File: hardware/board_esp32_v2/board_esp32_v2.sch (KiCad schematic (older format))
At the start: 96 parts, among them J1 USB_B_Micro, J2 Conn_01x02, J3 Micro_SD_Card_Det_Hirose_DM3AT, Q1 AO3401, Q2 AO3400, Q3 AO3401, SW1 SW_Push-Std, U1 FT231XS, U2 ESP32-WROOM-32D, U3 E22-900M22S, U4 E22-900M30S, U5 TPS62162DGK

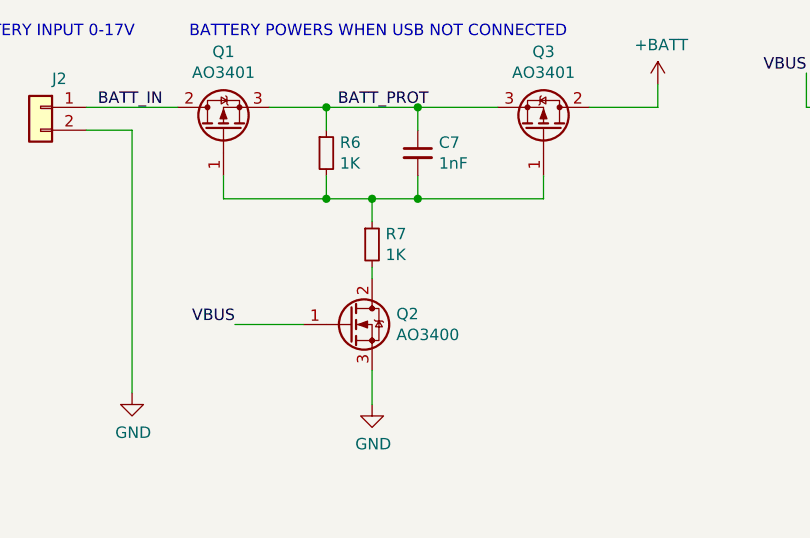
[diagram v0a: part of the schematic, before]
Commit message: Finish implementing fixes and pin changes for board_esp32_v2.
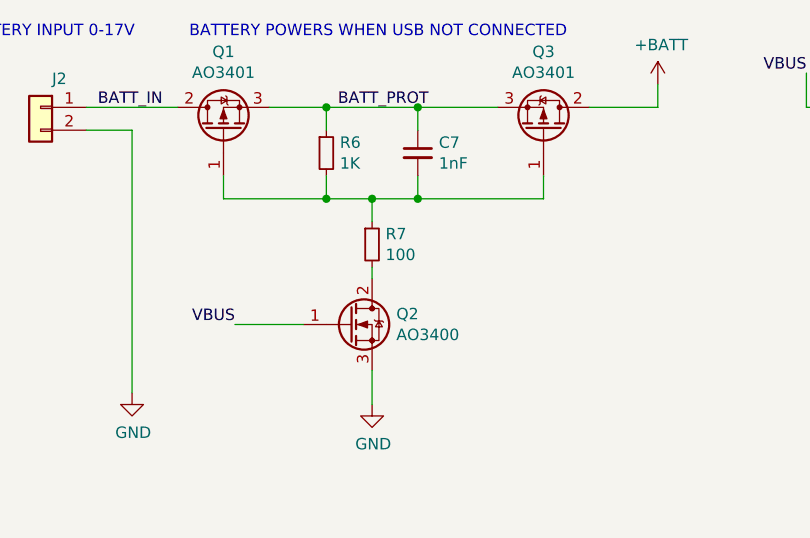
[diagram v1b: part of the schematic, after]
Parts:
- R7: value 1K -> 100
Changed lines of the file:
@@
-EESchema Schematic File Version 5
-EELAYER 32 0
+EESchema Schematic File Version 4
+EELAYER 30 0
 EELAYER END
 $Descr A3 16535 11693
@@
 Comment3 ""
 Comment4 ""
-Comment5 ""
-Comment6 ""
-Comment7 ""
-Comment8 ""
-Comment9 ""
 $EndDescr
 Connection ~ 13100 1350
@@
 P 4750 1650
 F 0 "R7" H 4809 1696 50  0000 L CNN
-F 1 "1K" H 4809 1605 50  0000 L CNN
+F 1 "100" H 4809 1605 50  0000 L CNN
 F 2 "Resistor_SMD:R_0402_1005Metric" H 4750 1650 50  0001 C CNN
 F 3 "~" H 4750 1650 50  0001 C CNN

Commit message: adds board_esp32_v3
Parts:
- removed U2: ESP32-WROOM-32D, RF_Module:ESP32-WROOM-32, symbol RF_Module:ESP32-WROOM-32D
- added JP42: SolderJumper_2_Open, Jumper:SolderJumper-2_P1.3mm_Open_RoundedPad1.0x1.5mm, symbol Jumper:SolderJumper_2_Open
- added TP5, TP6, TP7, TP8: TP_HOLE, Connector_PinHeader_2.54mm:PinHeader_1x01_P2.54mm_Vertical, symbol fitz_parts:TP_HOLE
- added U2: ESP32-WROOM-32U, RF_Module:ESP32-WROOM-32U, symbol RF_Module:ESP32-WROOM-32U
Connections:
- net labels removed: LORA1_TXEN, LORA2_TXEN
- wire segments 284 -> 290
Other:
- note added: "Possible Connection\nto save GPIO"
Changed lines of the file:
@@
-EESchema Schematic File Version 4
-EELAYER 30 0
+EESchema Schematic File Version 5
+EELAYER 34 0
 EELAYER END
 $Descr A3 16535 11693
@@
 Comment3 ""
 Comment4 ""
+Comment5 ""
+Comment6 ""
+Comment7 ""
+Comment8 ""
+Comment9 ""
 $EndDescr
+Connection ~ 1150 3900
+Connection ~ 1200 7400
+Connection ~ 1200 8000
+Connection ~ 1250 1750
+Connection ~ 1300 4000
+Connection ~ 1700 7350
+Connection ~ 1700 7400
+Connection ~ 2550 7150
+Connection ~ 2600 3000
+Connection ~ 2600 5400
+Connection ~ 3000 6450
+Connection ~ 3000 7150
+Connection ~ 3500 3000
+Connection ~ 3500 5000
+Connection ~ 3750 6450
+Connection ~ 4550 1050
+Connection ~ 4550 1450
+Connection ~ 4750 1450
+Connection ~ 4800 7150
+Connection ~ 4800 7350
+Connection ~ 4950 1050
+Connection ~ 4950 1450
+Connection ~ 5150 9350
+Connection ~ 5350 8350
+Connection ~ 5350 8450
+Connection ~ 5350 8750
+Connection ~ 8250 3450
+Connection ~ 8250 6200
+Connection ~ 8250 6250
+Connection ~ 8850 3450
+Connection ~ 8850 6200
+Connection ~ 11500 1350
+Connection ~ 11700 1350
+Connection ~ 12150 2150
+Connection ~ 12250 2150
+Connection ~ 12500 4950
 Connection ~ 13100 1350
 Connection ~ 13350 1350
 Connection ~ 13900 1350
-Connection ~ 11700 1350
-Connection ~ 11500 1350
-Connection ~ 12500 4950
-Connection ~ 8250 6250
-Connection ~ 8850 6200
-Connection ~ 8250 6200
-Connection ~ 8850 3450
-Connection ~ 8250 3450
-Connection ~ 1250 1750
-Connection ~ 2600 3000
-Connection ~ 1300 4000
-Connection ~ 1150 3900
-Connection ~ 3500 3000
-Connection ~ 4950 1050
-Connection ~ 4550 1050
-Connection ~ 4950 1450
-Connection ~ 4750 1450
-Connection ~ 4550 1450
-Connection ~ 3500 5000
-Connection ~ 2600 5400
-Connection ~ 3000 6450
-Connection ~ 3000 7150
-Connection ~ 2900 7150
-Connection ~ 3750 6450
-Connection ~ 4800 7150
-Connection ~ 4800 7350
-Connection ~ 5150 9350
-Connection ~ 5350 8750
-Connection ~ 1200 8000
-Connection ~ 1700 7350
-Connection ~ 1200 7400
-Connection ~ 1700 7400
-Connection ~ 5350 8450
-Connection ~ 5350 8350
-Connection ~ 12150 2150
-Connection ~ 12250 2150
+NoConn ~ 3150 8550
 NoConn ~ 9600 7450
+NoConn ~ 3150 8350
 NoConn ~ 9600 4700
+NoConn ~ 3150 8450
+NoConn ~ 3150 8850
 NoConn ~ 3150 8750
-NoConn ~ 3150 8850
-NoConn ~ 3150 8350
-NoConn ~ 3150 8450
-NoConn ~ 3150 8550
 NoConn ~ 3150 8650
 Wire Wire Line
@@
 	2150 1750 2150 1850
 Wire Wire Line
+	2350 7150 2550 7150
+Wire Wire Line
 	2400 1050 2400 1450
 Wire Wire Line
 	2400 1850 2400 1750
 Wire Wire Line
-	2500 7150 2900 7150
+	2550 7150 2550 7350
+Wire Wire Line
+	2550 7150 3000 7150
+Wire Wire Line
+	2550 7350 2300 7350
 Wire Wire Line
 	2600 2900 2600 3000
@@
 	2800 5400 2600 5400
 Wire Wire Line
-	2900 7150 2900 7350
-Wire Wire Line
-	2900 7150 3000 7150
-Wire Wire Line
-	2900 7350 2300 7350
-Wire Wire Line
 	3000 6350 3000 6450
 Wire Wire Line
@@
 	3000 7150 3150 7150
 Wire Wire Line
+	3000 7350 3150 7350
+Wire Wire Line
+	3000 7450 3150 7450
+Wire Wire Line
 	3400 3600 3500 3600
 Wire Wire Line
@@
 	6000 950  6000 1050
 Wire Wire Line
+	6150 5550 6150 5650
+Wire Wire Line
+	6150 5650 6250 5650
+Wire Wire Line
 	6650 900  6650 1050
 Wire Wire Line
 	6650 1050 6850 1050
+Wire Wire Line
+	6650 5550 6650 5650
+Wire Wire Line
+	6650 5650 6550 5650
 Wire Wire Line
 	7150 1050 7350 1050
@@
 Text Notes 4500 6550 0    50   ~ 0
 TODO: \n-DOUBLE CHECK RX/TX dir\n-set BATT div to match battery\n- DOUBLE CHECK SPI CS
+Text Notes 5700 5350 0    50   ~ 0
+Possible Connection\nto save GPIO
 Text Notes 8000 5600 0    50   ~ 0
 NOTE: E22-900M22S MAX CURRENT 119mA\nVin 1.8-3.7V
@@
 Text Label 1900 3650 2    50   ~ 0
 FT_3V3
-Text Label 2500 7150 2    50   ~ 0
+Text Label 2350 7150 2    50   ~ 0
 FT_RTS
 Text Label 2800 3000 0    50   ~ 0
@@
 LORA1_NSS
 Text Label 4450 8250 0    50   ~ 0
-LORA2_DIO2
+LORA2_DIO1
 Text Label 4450 8350 0    50   ~ 0
 VSPI_CLK
@@
 VSPI_MISO
 Text Label 4450 8550 0    50   ~ 0
-LORA1_DIO2
+LORA2_RXEN
 Text Label 4450 8650 0    50   ~ 0
 LORA1_BUSY
 Text Label 4450 8750 0    50   ~ 0
 VSPI_MOSI
-Text Label 4450 8850 0    50   ~ 0
-LORA1_TXEN
 Text Label 4450 8950 0    50   ~ 0
-LORA2_RXEN
+LORA1_DIO1
 Text Label 4450 9050 0    50   ~ 0
 LORA1_RXEN
-Text Label 4450 9150 0    50   ~ 0
-LORA2_TXEN
 Text Label 4450 9250 0    50   ~ 0
 LORA2_NSS
@@
 Text Label 5500 8850 0    50   ~ 0
 LORA2_MOSI
+Text Label 6150 5550 2    50   ~ 0
+LORA1_DIO1
 Text Label 6650 900  2    50   ~ 0
 VBUS
+Text Label 6650 5550 0    50   ~ 0
+LORA2_DIO1
 Text Label 7350 9400 0    50   ~ 0
 ESP_LED
@@
 LORA1_RXEN
 Text Label 7550 4250 2    50   ~ 0
-LORA1_TXEN
+LORA1_DIO2
 Text Label 7550 4500 2    50   ~ 0
 LORA1_MOSI
@@
 LORA2_RXEN
 Text Label 7700 7000 2    50   ~ 0
-LORA2_TXEN
+LORA2_DIO2
 Text Label 7700 7250 2    50   ~ 0
 LORA2_MOSI
@@
 LORA2_NSS
 Text Label 8000 9400 0    50   ~ 0
-LORA1_DIO1
+LORA1_DIO2
 Text Label 8650 9400 0    50   ~ 0
-LORA2_DIO1
+LORA2_DIO2
 Text Label 10050 6900 0    50   ~ 0
 LORA2_DIO1
@@
 $EndComp
 $Comp
+L fitz_parts:TP_HOLE TP5
+U 1 1 00000000
+P 3000 7350
+F 0 "TP5" V 3000 7650 50  0000 C CNN
+F 1 "TP_HOLE" H 3000 7550 50  0001 C CNN
+F 2 "Connector_PinHeader_2.54mm:PinHeader_1x01_P2.54mm_Vertical" H 3200 7350 50  0001 C CNN
+F 3 "~" H 3200 7350 50  0001 C CNN
+	1    3000 7350
+	0    -1   -1   0
+$EndComp
+$Comp
+L fitz_parts:TP_HOLE TP6
+U 1 1 00000000
+P 3000 7450
+F 0 "TP6" V 3000 7750 50  0000 C CNN
+F 1 "TP_HOLE" H 3000 7650 50  0001 C CNN
+F 2 "Connector_PinHeader_2.54mm:PinHeader_1x01_P2.54mm_Vertical" H 3200 7450 50  0001 C CNN
+F 3 "~" H 3200 7450 50  0001 C CNN
+	1    3000 7450
+	0    -1   -1   0
+$EndComp
+$Comp
 L Connector:TestPoint TP1
 U 1 1 5DCF71F0
@@
 $EndComp
 $Comp
+L fitz_parts:TP_HOLE TP7
+U 1 1 00000000
+P 4450 8850
+F 0 "TP7" V 4400 9100 50  0000 C CNN
+F 1 "TP_HOLE" H 4450 9050 50  0001 C CNN
+F 2 "Connector_PinHeader_2.54mm:PinHeader_1x01_P2.54mm_Vertical" H 4650 8850 50  0001 C CNN
+F 3 "~" H 4650 8850 50  0001 C CNN
+	1    4450 8850
+	0    1    1    0
+$EndComp
+$Comp
+L fitz_parts:TP_HOLE TP8
+U 1 1 00000000
+P 4450 9150
+F 0 "TP8" V 4400 9400 50  0000 C CNN
+F 1 "TP_HOLE" H 4450 9350 50  0001 C CNN
+F 2 "Connector_PinHeader_2.54mm:PinHeader_1x01_P2.54mm_Vertical" H 4650 9150 50  0001 C CNN
+F 3 "~" H 4650 9150 50  0001 C CNN
+	1    4450 9150
+	0    1    1    0
+$EndComp
+$Comp
 L power:+3V3 #PWR0130
 U 1 1 5DCBEDF2
@@
 $EndComp
 $Comp
+L Jumper:SolderJumper_2_Open JP42
+U 1 1 00000000
+P 6400 5650
+F 0 "JP42" V 6392 5392 50  0000 L CNN
+F 1 "SolderJumper_2_Open" V 6487 5695 50  0001 R CNN
+F 2 "Jumper:SolderJumper-2_P1.3mm_Open_RoundedPad1.0x1.5mm" H 6400 5650 50  0001 C CNN
+F 3 "~" H 6400 5650 50  0001 C CNN
+	1    6400 5650
+	1    0    0    -1
+$EndComp
+$Comp
 L Jumper:SolderJumper_2_Bridged JP13
 U 1 1 5DD60A96
@@
 $EndComp
 $Comp
-L RF_Module:ESP32-WROOM-32D U2
-U 1 1 5DB8779E
+L RF_Module:ESP32-WROOM-32U U2
+U 1 1 00000000
 P 3750 8350
-F 0 "U2" H 3750 8750 50  0000 C CNN
-F 1 "ESP32-WROOM-32D" H 4250 6950 50  0000 C CNN
-F 2 "RF_Module:ESP32-WROOM-32" H 3750 6850 50  0001 C CNN
+F 0 "U2" H 3750 9926 50  0000 C CNN
+F 1 "ESP32-WROOM-32U" H 3750 9835 50  0000 C CNN
+F 2 "RF_Module:ESP32-WROOM-32U" H 3750 6850 50  0001 C CNN
 F 3 "https://www.espressif.com/sites/default/files/documentation/esp32-wroom-32d_esp32-wroom-32u_datasheet_en.pdf" H 3450 8400 50  0001 C CNN
 	1    3750 8350
